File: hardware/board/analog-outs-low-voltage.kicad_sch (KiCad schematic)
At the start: 14 parts

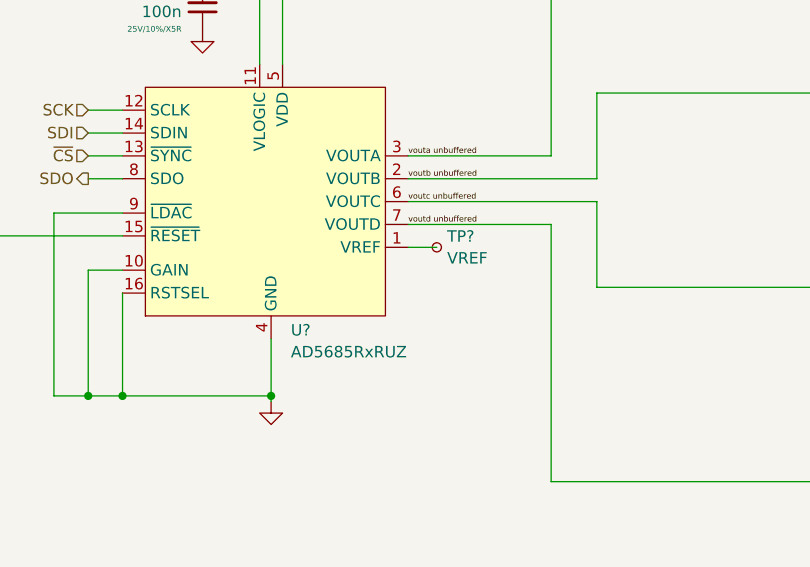
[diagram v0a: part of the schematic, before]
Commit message: Update resistor values in Vout DAC buffers
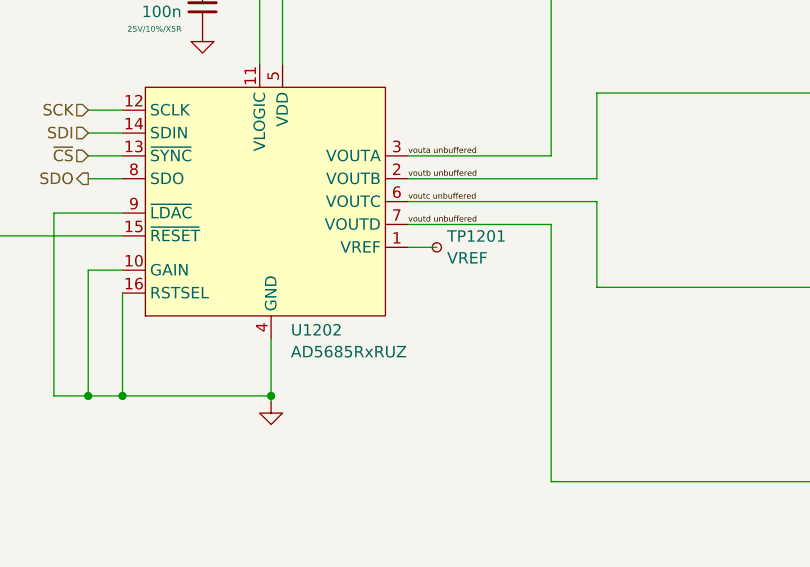
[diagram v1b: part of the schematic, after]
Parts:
- gave numbers to parts that had none: 2
